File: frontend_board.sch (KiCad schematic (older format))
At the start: 122 parts, among them J1 Conn_02x20_Odd_Even, J2 Conn_02x10_Odd_Even, J3 Conn_02x20_Odd_Even, U1 ADS1299_TQFP, U2 ADM7170, U3 LD1117S50TR_SOT223

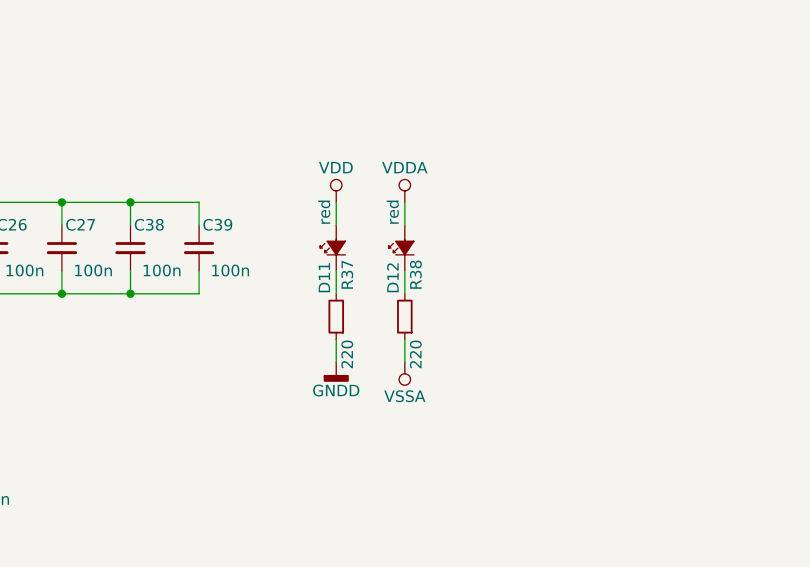
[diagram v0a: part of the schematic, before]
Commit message: frontend: Reshape to 60x70mm, fixup silk
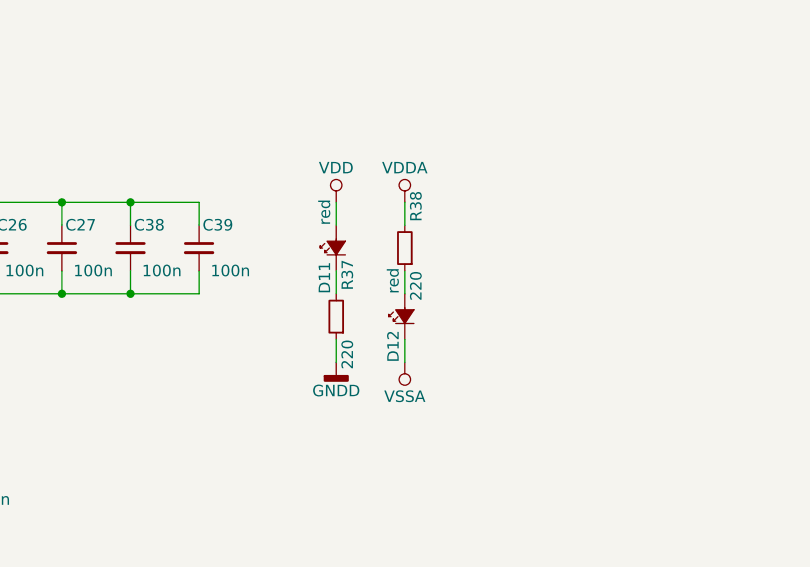
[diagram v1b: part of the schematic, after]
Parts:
- C10, C11, C12, C3, C6, C7, C8, C9: footprint Capacitors_SMD:C_0402 -> Capacitors_SMD:C_0402_NoSilk
- D2, D3, D8, D9: footprint TO_SOT_Packages_SMD:SOT-363_SC-70-6 -> footprints:SOT-363_SC-70-6-nosilk
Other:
- moved on the sheet: D12, R38

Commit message: Add cable breakout board
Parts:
- J1: value Conn_02x20_Odd_Even -> Bergstak 20P female 3.7mm; Digikey PN (none) -> 609-5429-1-ND; Digikey URL (none) -> https://www.digikey.com/product-detail/en/amphenol-fci/1014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; Mating (none) -> Amphenol 10144518-042802LF; Mfg (none) -> Amphenol; Mfg PN (none) -> 10144517-041802LF
- J3: Digikey PN (none) -> 609-5429-1-ND; Digikey URL (none) -> https://www.digikey.com/product-detail/en/amphenol-fci/1014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; Mating (none) -> Amphenol 10144518-042802LF; Mfg (none) -> Amphenol; Mfg PN (none) -> 10144517-041802LF
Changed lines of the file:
@@
 P 3250 2150
 F 0 "J1" H 3300 3150 50  0000 C CNN
-F 1 "Conn_02x20_Odd_Even" H 3300 1050 50  0000 C CNN
+F 1 "Bergstak 20P female 3.7mm" H 3300 1050 50  0000 C CNN
 F 2 "footprints:bergstak_receptacle1_2x20_female" H 3250 2150 50  0001 C CNN
-F 3 "" H 3250 2150 50  0001 C CNN
+F 3 "https://cdn.amphenol-icc.com/media/wysiwyg/files/drawing/10144517.pdf" H 3250 2150 50  0001 C CNN
+F 4 "10144517-041802LF" H 3250 2150 60  0001 C CNN "Mfg PN"
+F 5 "Amphenol" H 3250 2150 60  0001 C CNN "Mfg"
+F 6 "609-5429-1-ND" H 3250 2150 60  0001 C CNN "Digikey PN"
+F 7 "https://www.digikey.com/product-detail/en/amphenol-fci/10144517-041802LF/609-5429-1-ND/8573002" H 3250 2150 60  0001 C CNN "Digikey URL"
+F 8 "Amphenol 10144518-042802LF" H 3250 2150 60  0001 C CNN "Mating"
 	1    3250 2150
 	0    -1   1    0
@@
 F 1 "Conn_02x20_Odd_Even" V 3850 6300 50  0001 C CNN
 F 2 "footprints:bergstak_receptacle1_2x20_female" H 3350 5900 50  0001 C CNN
-F 3 "" H 3350 5900 50  0001 C CNN
+F 3 "https://cdn.amphenol-icc.com/media/wysiwyg/files/drawing/10144517.pdf" H 3350 5900 50  0001 C CNN
+F 4 "10144517-041802LF" H 3350 5900 60  0001 C CNN "Mfg PN"
+F 5 "Amphenol" H 3350 5900 60  0001 C CNN "Mfg"
+F 6 "609-5429-1-ND" H 3350 5900 60  0001 C CNN "Digikey PN"
+F 7 "https://www.digikey.com/product-detail/en/amphenol-fci/10144517-041802LF/609-5429-1-ND/8573002" H 3350 5900 60  0001 C CNN "Digikey URL"
+F 8 "Amphenol 10144518-042802LF" H 3350 5900 60  0001 C CNN "Mating"
 	1    3350 5900
 	0    1    -1   0
